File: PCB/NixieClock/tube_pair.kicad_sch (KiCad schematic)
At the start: 5 parts, among them U1 PCF8574, U2 K155ND1, U3 K155ND1

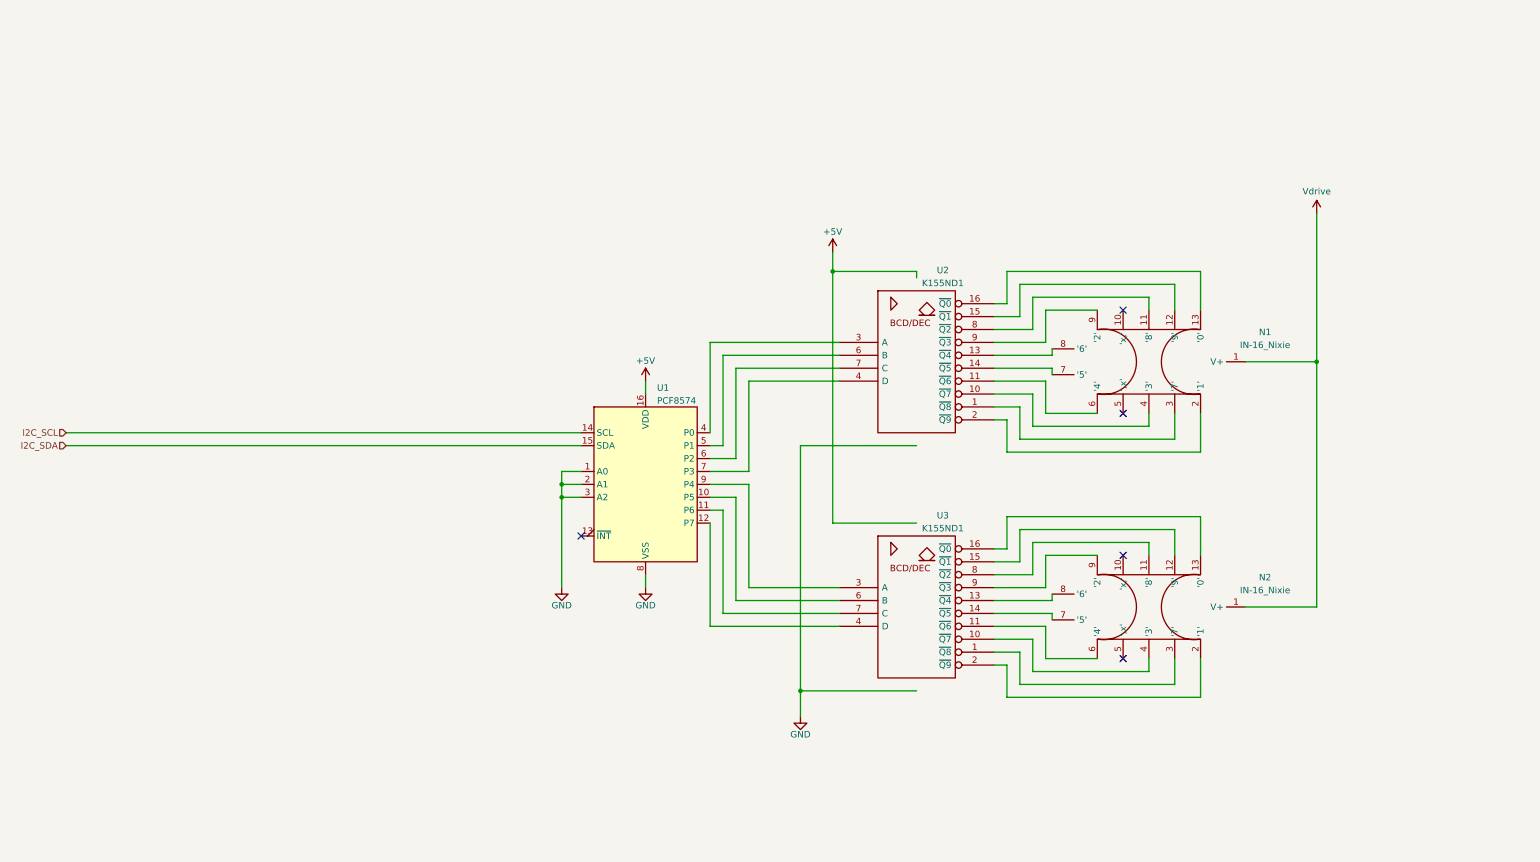
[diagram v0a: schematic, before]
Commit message: nixie panel PCB layout progress
laid out tube 1 with top and bottom traces. added GND polygon on both sides, with exception zone around tube 1. tubes 2-4 to be laid out with top and bottom traces
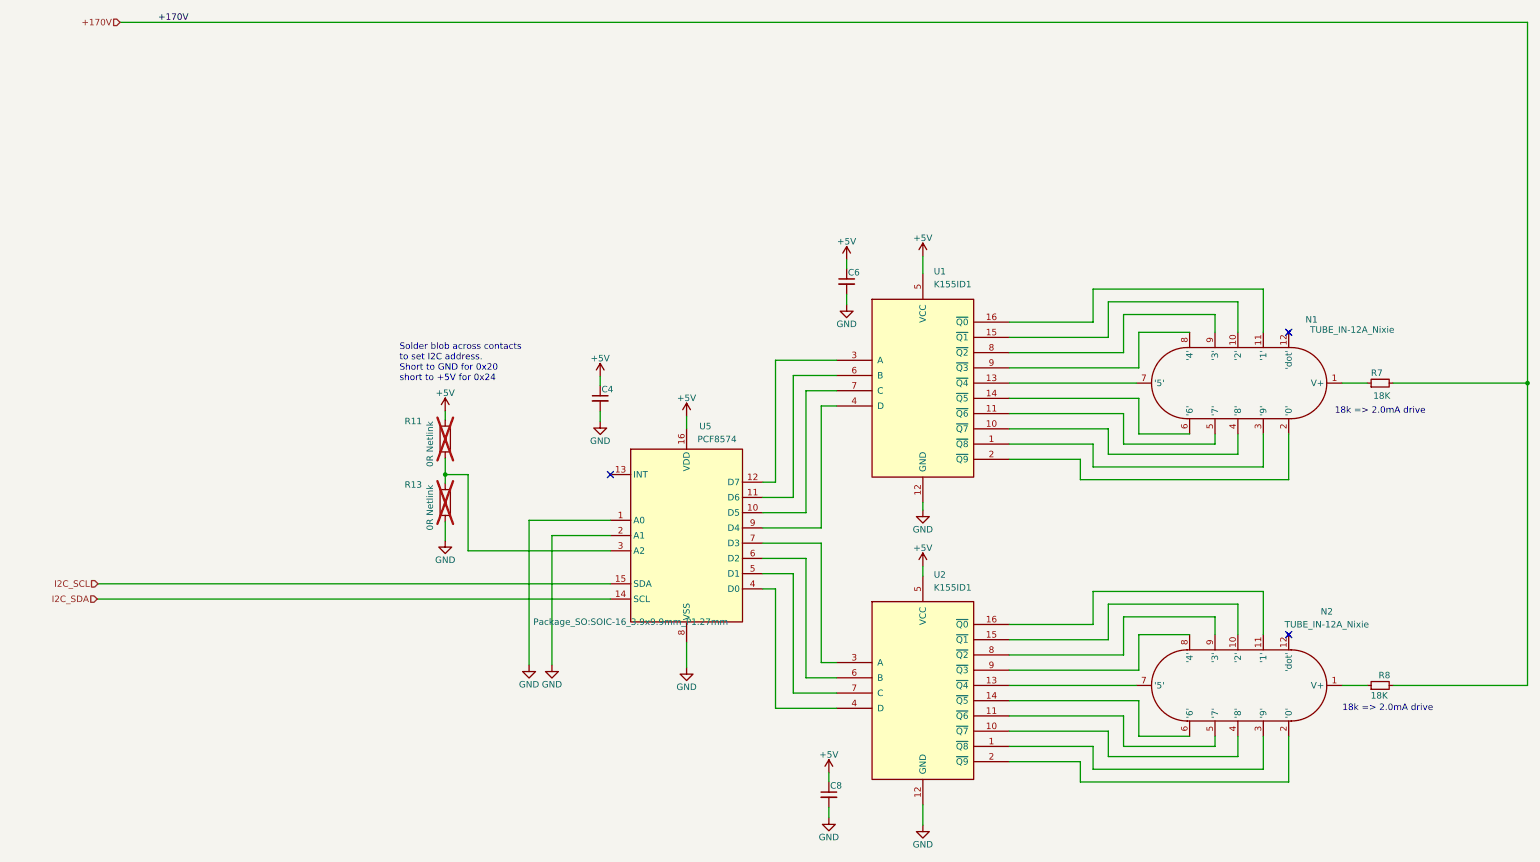
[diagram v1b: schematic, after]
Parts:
- removed N1, N2: IN-16_Nixie, TerminalCuriosityFootprints:IN-16_Nixie_Tube, symbol TerminalCuriositySymbols:IN-16_Nixie
- removed U1: PCF8574, Package_SO:SOIC-16W_7.5x10.3mm_P1.27mm, symbol Interface_Expansion:PCF8574
- removed U2, U3: K155ND1, Package_DIP:DIP-16_W7.62mm, symbol 74xx_IEEE:74141
- added C4, C6, C8: 100nF, Capacitor_SMD:C_0603_1608Metric_Pad1.08x0.95mm_HandSolder, symbol Device:C_Small
- added N1, N2: TUBE_IN-12A_Nixie, TerminalCuriosityFootprints:in-12_nixie-tube, symbol TerminalCuriositySymbols:TUBE_IN-12A_Nixie
- added R11, R13: 0R Netlink, Resistor_SMD:R_0402_1005Metric, symbol Device:R
- added R7, R8: 18K, Resistor_SMD:R_0805_2012Metric_Pad1.20x1.40mm_HandSolder, symbol Device:R_Small
- added U1, U2: K155ID1, Package_DIP:DIP-16_W7.62mm, symbol TerminalCuriositySymbols:IC_K155ID1_TUBE_DRIVER
- added U5: PCF8574, Package_SO:SOIC-16_3.9x9.9mm_P1.27mm, symbol TerminalCuriositySymbols:IC_PCF8574
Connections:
- net +5V: now also C4.1, C6.1, C8.1, R11.1, U1.5 (VCC), U2.5 (VCC), U5.16 (VDD)
- net GND: now also C4.2, C6.2, C8.2, R13.2, U1.12 (GND), U2.12 (GND), U5.1 (A0), U5.2 (A1), U5.8 (VSS)
- net I2C_SCL: now also U5.15 (SDA)
- net I2C_SDA: now also U5.14 (SCL)
- new net: N2.3 ('9'), U2.1 (~{Q8})
- new net: N2.4 ('8'), U2.10 (~{Q7})
- new net: N2.5 ('7'), U2.11 (~{Q6})
- new net: N2.7 ('5'), U2.13 (~{Q4})
- new net: N2.6 ('6'), U2.14 (~{Q5})
- new net: N2.10 ('2'), U2.15 (~{Q1})
- new net: N2.11 ('1'), U2.16 (~{Q0})
- new net: N2.2 ('0'), U2.2 (~{Q9})
- new net: U2.3 (A), U5.7 (D3)
- new net: U2.4 (D), U5.4 (D0)
- new net: U2.6 (B), U5.6 (D2)
- new net: U2.7 (C), U5.5 (D1)
- new net: N2.9 ('3'), U2.8 (~{Q2})
- new net: N2.8 ('4'), U2.9 (~{Q3})
- new net: N1.1 (V+), R7.1
- new net: N1.10 ('2'), U1.15 (~{Q1})
- new net: N1.11 ('1'), U1.16 (~{Q0})
- new net: N1.2 ('0'), U1.2 (~{Q9})
- new net: N1.3 ('9'), U1.1 (~{Q8})
- new net: N1.4 ('8'), U1.10 (~{Q7})
- new net: N1.5 ('7'), U1.11 (~{Q6})
- new net: N1.6 ('6'), U1.14 (~{Q5})
- new net: N1.7 ('5'), U1.13 (~{Q4})
- new net: N1.8 ('4'), U1.9 (~{Q3})
- new net: N1.9 ('3'), U1.8 (~{Q2})
- new net: N2.1 (V+), R8.1
- new net: R11.2, R13.1, U5.3 (A2)
- new net: U1.7 (C), U5.10 (D5)
- new net: U1.6 (B), U5.11 (D6)
- new net: U1.3 (A), U5.12 (D7)
- new net: U1.4 (D), U5.9 (D4)
- new net +170V: R7.2, R8.2
- no-connect marks 5 -> 3
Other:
- note added: "18k => 2.0mA drive"
- note added: "Solder blob across contacts to set I2C address. Short to GND for 0x20 short to +5V for 0x24"
